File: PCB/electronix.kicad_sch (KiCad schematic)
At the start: 86 parts, among them IC1 DRV8210DRLR, IC2 DRV8210DRLR, IC3 AP9101CK6-ANTRG1, IC4 ICM-20602, J1 USB-C 6pin, J2 PRG, M1 N20 motor, M2 N20 motor, Q1 757-SSM6N7002KFULF, Q2 757-SSM6N7002KFULF, Q3 Phototransistor, Q4 Phototransistor, Q5 Phototransistor, Q6 Phototransistor, Q7 757-SSM6N7002KFULF, Q8 UMH3N FHA, SW1 RESET, U2 MCP73213-A6SI/MF, U3 ESP32-WROOM-32, U4 LMR51420YDDRCR

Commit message: Add start button General schematic edits Add Mouser BOM
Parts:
- removed R25, R26, R27: 10k, symbol Device:R
- added C22: 4u7/50V, symbol Device:C
- added D7, D8: LED, symbol Device:LED
- added R11: 100k 1%, Resistor_SMD:R_0603_1608Metric, symbol Device:R
- added R12: 22k1 1%, Resistor_SMD:R_0603_1608Metric, symbol Device:R
- added R36, R37: 330R, symbol Device:R
- added R5: 10k, symbol Device:R
- added SW2: SW_DIP_x01, symbol Switch:SW_DIP_x01
- added SW3: START, symbol Switch:SW_Push
- L1: value 4u7 -> 3u3
- renumbered C21 to C1, C3 to C10, C1 to C11, C4 to C12, C5 to C16, C6 to C17, C14 to C2, C19 to C3, C20 to C4, C17 to C5, C16 to C6, C15 to C7, C18 to C8, C2 to C9, D6 to D1, D1 to D2, D2 to D3, D3 to D5, D4 to D6, IC4 to IC1, IC3 to IC2, IC1 to IC3, IC2 to IC4, Q8 to Q1, Q7 to Q2, Q2 to Q3, Q6 to Q5, Q1 to Q6, Q3 to Q7, Q5 to Q8, R30 to R1, R23 to R10, R24 to R11, R22 to R12, R5 to R13, R7 to R14, R6 to R15, R8 to R16, R28 to R17, R1 to R18, R2 to R19, R35 to R2, R34 to R20, R33 to R21, R3 to R22, R4 to R23, R9 to R24, R10 to R25, R11 to R28, R12 to R29, R31 to R30, R32 to R31, R13 to R32, R14 to R33, R15 to R34, R16 to R35, R29 to R6, R19 to R7, R20 to R8, R21 to R9, U2 to U1, U3 to U2
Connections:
- net +3V3: now also C10.1, C5.1, C6.1, C7.2, C8.1, C9.1, D1.1 (K), IC3.5 (VM), IC4.5 (VM), M1.2 (Pin_2), M2.2 (Pin_2), R17.2, SW1.2, U4.3 (VIN), U4.5 (EN), D8.2 (A), R11.1, R5.1, SW2.1
- net +BATT: now also SW2.2; no longer C10.1, C5.1, C6.1, C7.2, C8.1, C9.1, D1.1 (K), IC3.5 (VM), IC4.5 (VM), M1.2 (Pin_2), M2.2 (Pin_2), R17.2, SW1.2, U4.3 (VIN), U4.5 (EN)
- net GND: now also C22.2, R12.2, R36.1, R37.1, SW3.1
- net v_sense: now also R11.2, R12.1
- net ST: now reaches U2.30 (IO18)
- net ST: now also C22.1, R5.2, SW3.2
- net at U2.37 (IO23): now also D7.2 (A)
- new net: D8.1 (K), R37.2
- new net: D7.1 (K), R36.2
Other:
- note added: "START"
- moved on the sheet: C2, C5, C8, D1, J2, R1, R17, R6, SW1

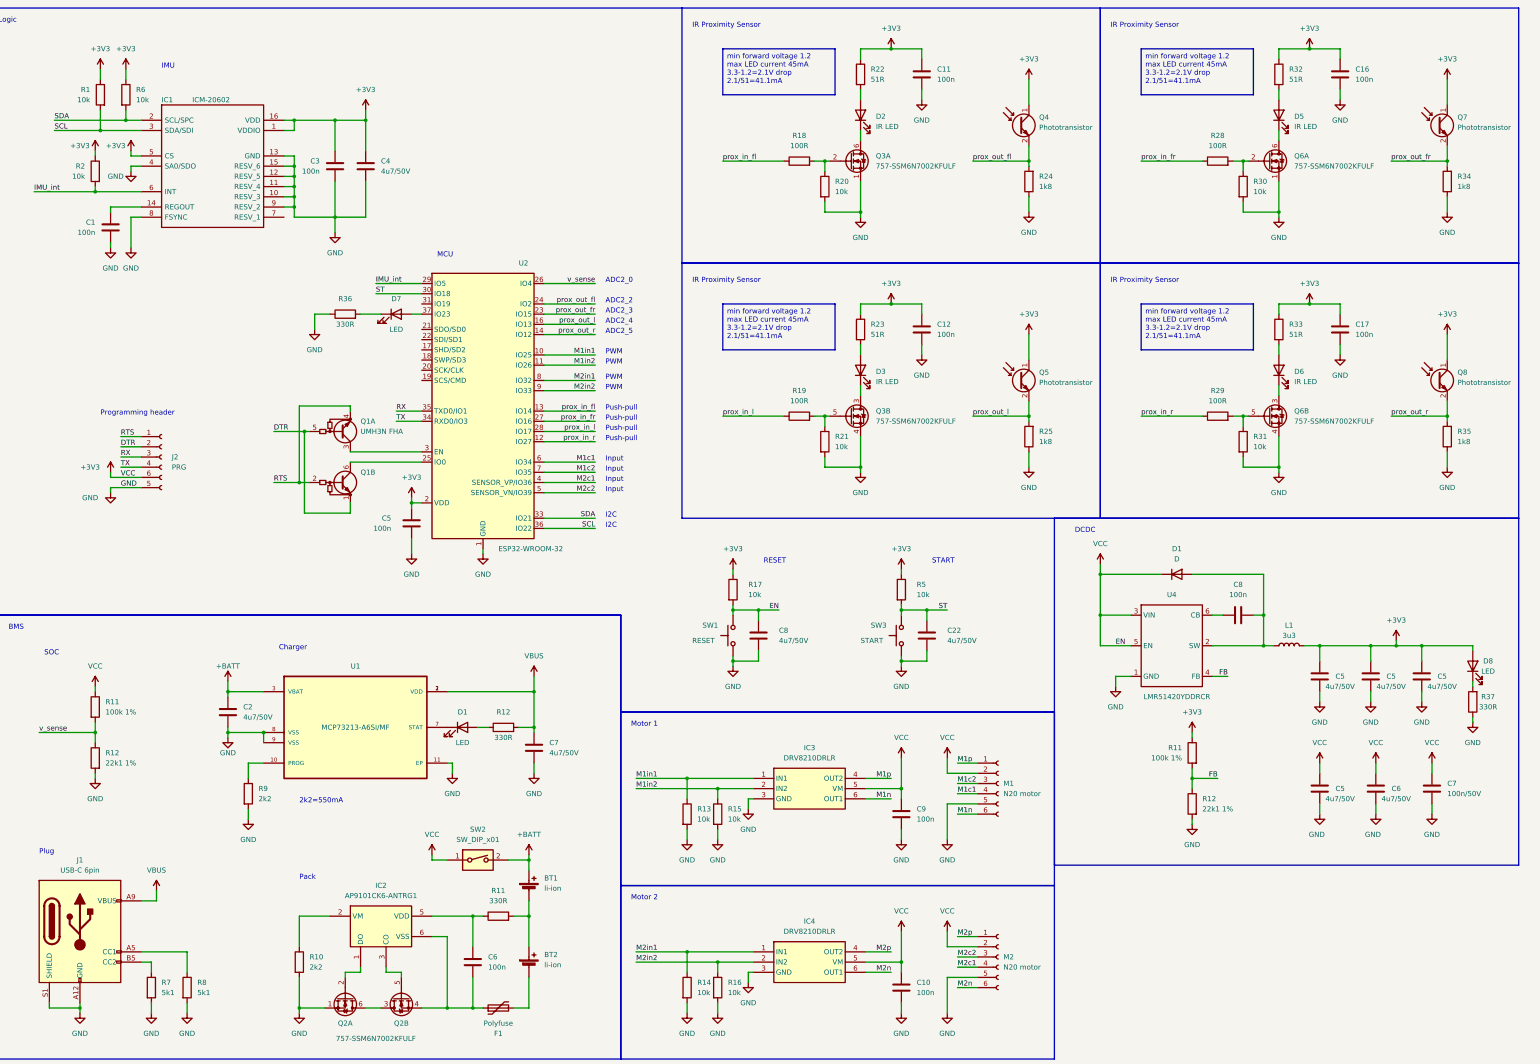
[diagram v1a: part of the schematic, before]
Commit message: Assign fooprints Finish BOM Fix libraries Generic footprints where applicable ERC - remove erroneous net labels Start working on layout
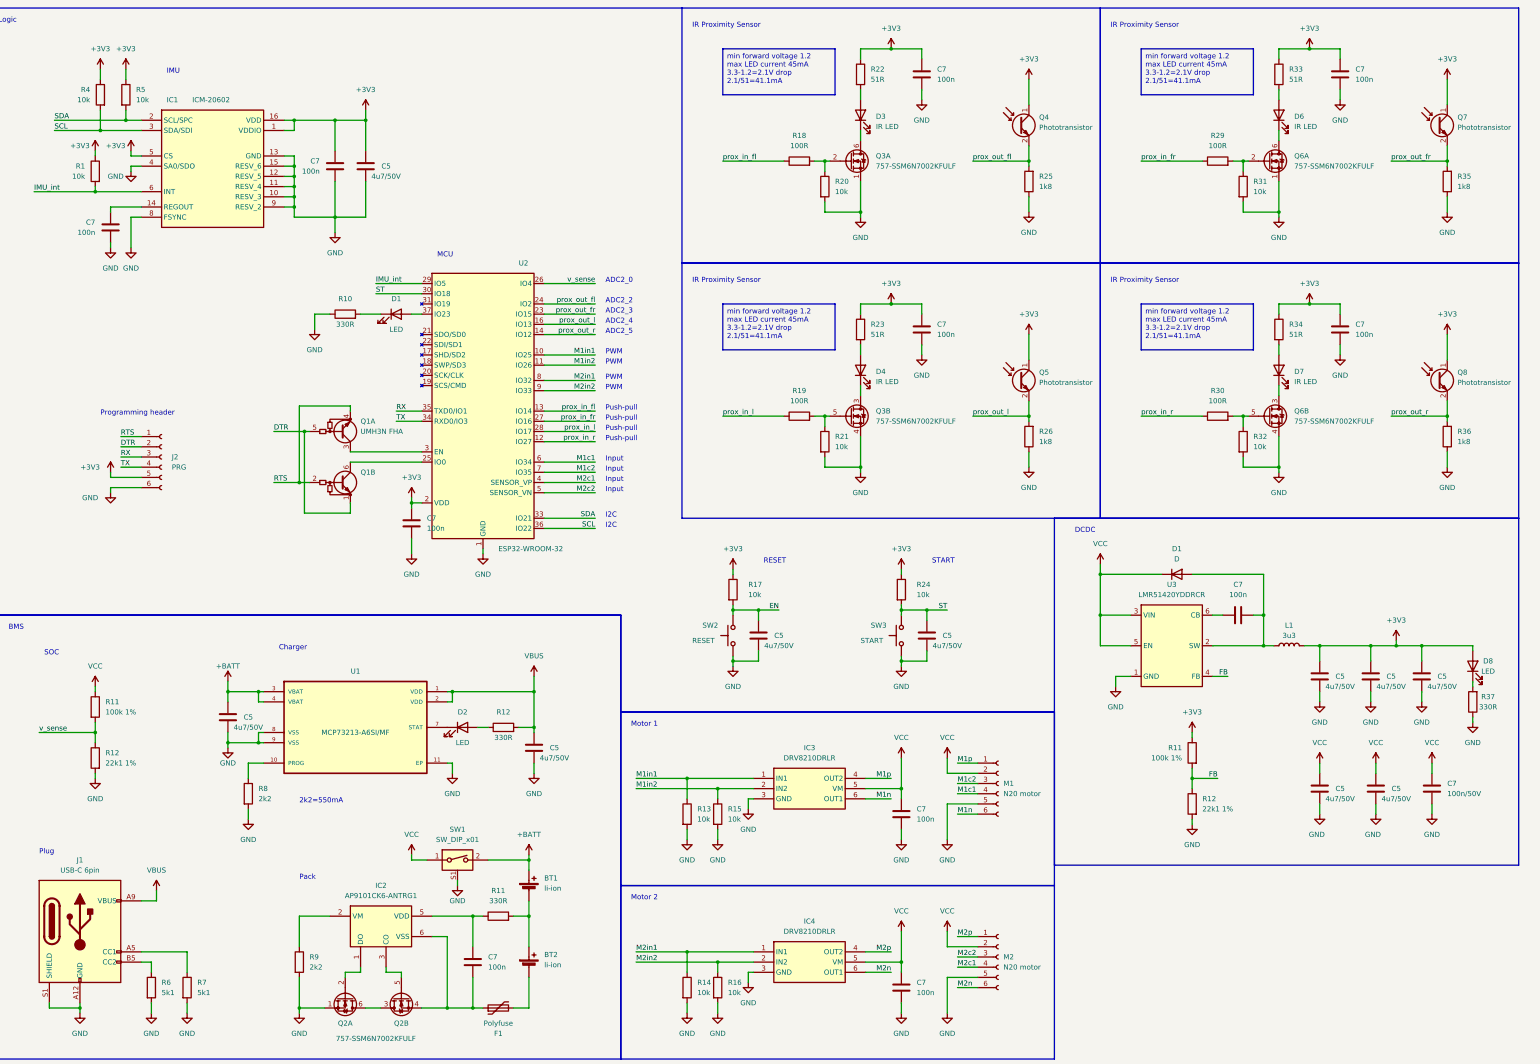
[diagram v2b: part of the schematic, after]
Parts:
- removed C1, C10, C11, C12, C16, C17, C3, C5, C6, C8, C9: 100n, symbol Device:C
- removed C2, C22, C4, C7, C8: 4u7/50V, symbol Device:C
- removed C5 (x3), C6: 4u7/50V, Capacitor_SMD:C_1206_3216Metric, symbol Device:C
- removed U4: LMR51420YDDRCR, Package_TO_SOT_SMD:SOT-23-6, symbol parts:LMR51420
- added C5 (x9): 4u7/50V, Capacitor_SMD:C_0805_2012Metric, symbol Device:C
- added C7 (x11): 100n, Capacitor_SMD:C_0603_1608Metric, symbol Device:C
- added U3: LMR51420YDDRCR, Package_TO_SOT_SMD:SOT-23-6, symbol LMR51420:LMR51420
- BT1, BT2: footprint (none) -> Connector_JST:JST_XH_B2B-XH-AM_1x02_P2.50mm_Vertical
- C5: footprint Capacitor_SMD:C_1206_3216Metric -> Capacitor_SMD:C_0805_2012Metric
- D1: renamed from D7; footprint (none) -> LED_SMD:LED_0603_1608Metric
- D2: renamed from D1; footprint (none) -> LED_SMD:LED_0603_1608Metric
- D3: renamed from D2; footprint (none) -> LED_THT:LED_D5.0mm_Horizontal_O1.27mm_Z3.0mm
- D4: renamed from D3; footprint (none) -> LED_THT:LED_D5.0mm_Horizontal_O1.27mm_Z3.0mm
- D6: renamed from D5; footprint (none) -> LED_THT:LED_D5.0mm_Horizontal_O1.27mm_Z3.0mm
- D7: renamed from D6; footprint (none) -> LED_THT:LED_D5.0mm_Horizontal_O1.27mm_Z3.0mm
- D8: footprint (none) -> LED_SMD:LED_0603_1608Metric
- F1: footprint (none) -> Fuse:Fuse_1812_4532Metric
- IC1: footprint IAM20680HP -> Package_LGA:LGA-16_3x3mm_P0.5mm
- IC2: footprint SOT95P285X140-6N -> Package_TO_SOT_SMD:SOT-23-6
- IC3, IC4: footprint SOTFL50P160X60-6N -> Package_TO_SOT_SMD:SOT-563
- J1: footprint (none) -> 10164359-00011LF:1016435900011LF
- J2: footprint (none) -> Connector_PinHeader_2.54mm:PinHeader_1x06_P2.54mm_Vertical
- L1: footprint Inductor_SMD:L_Ferrocore_DLG-0705 -> Inductor_SMD:L_Changjiang_FNR5040S
- M1, M2: footprint (none) -> Connector_JST:JST_XH_B6B-XH-AM_1x06_P2.50mm_Vertical
- Q1, Q2, Q3, Q6: footprint (none) -> Package_TO_SOT_SMD:SOT-363_SC-70-6
- Q4, Q5, Q7, Q8: footprint (none) -> LED_THT:LED_D5.0mm_Horizontal_O1.27mm_Z3.0mm_IRBlack
- R1: renamed from R2; footprint (none) -> Resistor_SMD:R_0603_1608Metric
- R10: renamed from R36; footprint (none) -> Resistor_SMD:R_0603_1608Metric
- R11, R12, R13, R14, R15, R16, R17, R18, R19, R20, R21, R22, R23, R37: footprint (none) -> Resistor_SMD:R_0603_1608Metric
- R24: renamed from R5; footprint (none) -> Resistor_SMD:R_0603_1608Metric
- R25: renamed from R24; footprint (none) -> Resistor_SMD:R_0603_1608Metric
- R26: renamed from R25; footprint (none) -> Resistor_SMD:R_0603_1608Metric
- R29: renamed from R28; footprint (none) -> Resistor_SMD:R_0603_1608Metric
- R30: renamed from R29; footprint (none) -> Resistor_SMD:R_0603_1608Metric
- R31: renamed from R30; footprint (none) -> Resistor_SMD:R_0603_1608Metric
- R32: renamed from R31; footprint (none) -> Resistor_SMD:R_0603_1608Metric
- R33: renamed from R32; footprint (none) -> Resistor_SMD:R_0603_1608Metric
- R34: renamed from R33; footprint (none) -> Resistor_SMD:R_0603_1608Metric
- R35: renamed from R34; footprint (none) -> Resistor_SMD:R_0603_1608Metric
- R36: renamed from R35; footprint (none) -> Resistor_SMD:R_0603_1608Metric
- R4: renamed from R1; footprint (none) -> Resistor_SMD:R_0603_1608Metric
- R5: renamed from R6; footprint (none) -> Resistor_SMD:R_0603_1608Metric
- R6: renamed from R7; footprint (none) -> Resistor_SMD:R_0603_1608Metric
- R7: renamed from R8; footprint (none) -> Resistor_SMD:R_0603_1608Metric
- R8: renamed from R9; footprint (none) -> Resistor_SMD:R_0603_1608Metric
- R9: renamed from R10; footprint (none) -> Resistor_SMD:R_0603_1608Metric
- SW1: renamed from SW2; footprint (none) -> 1825232-1:18252321
- SW2: renamed from SW1; footprint (none) -> PTS636_SL50_LFS:PTS636SL50LFS
- SW3: footprint (none) -> PTS636_SL50_LFS:PTS636SL50LFS
- U1: footprint SON50P300X300X100-11N -> Package_DFN_QFN:DFN-10-1EP_3x3mm_P0.5mm_EP1.65x2.38mm_ThermalVias
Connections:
- net +3V3: now also J2.5 (Pin_5), C5.1, C5.1, C5.1, C7.2, C7.2, C7.2, C7.2, C7.2, C7.2; no longer C7.2, D1.1 (K), IC3.5 (VM), IC4.5 (VM), J2.6 (Pin_6), M1.2 (Pin_2), M2.2 (Pin_2), R11.1, R17.2, SW1.1, SW2.2
- net +BATT: now also U1.4 (VBAT), C5.1
- net FB: now also U3.4 (FB)
- net GND: now also J1.S2 (SHIELD), J1.S3 (SHIELD), J1.S4 (SHIELD), J2.6 (Pin_6), SW1.S1 (SHIELD), SW1.S2 (SHIELD), C5.2, C5.2, C5.2, C5.2, C5.2, C5.2, C5.2, C5.2, C5.2, C7.1, C7.1, C7.1, C7.1, C7.1, C7.1, C7.1, C7.1, C7.1, U3.1 (GND); no longer J2.5 (Pin_5)
- net ST: now also C5.1
- net VBUS: now also C5.1
- net at D1.2 (A), L1.1: now also C7.1, U3.2 (SW)
- net at IC2.5 (VDD), R11.1: now also C7.2
- net at IC1.14 (REGOUT): now also C7.2
- net at F1.1, IC2.6 (VSS), Q2.4 (S): now also C7.1
- new net: C7.2, U3.6 (CB)
- new net EN: C5.1, R17.2, SW2.2
- new net VCC: C5.1, C5.1, C7.2, C7.2, C7.2, D1.1 (K), IC3.5 (VM), IC4.5 (VM), M1.2 (Pin_2), M2.2 (Pin_2), R11.1, SW1.1, U3.3 (VIN), U3.5 (EN)

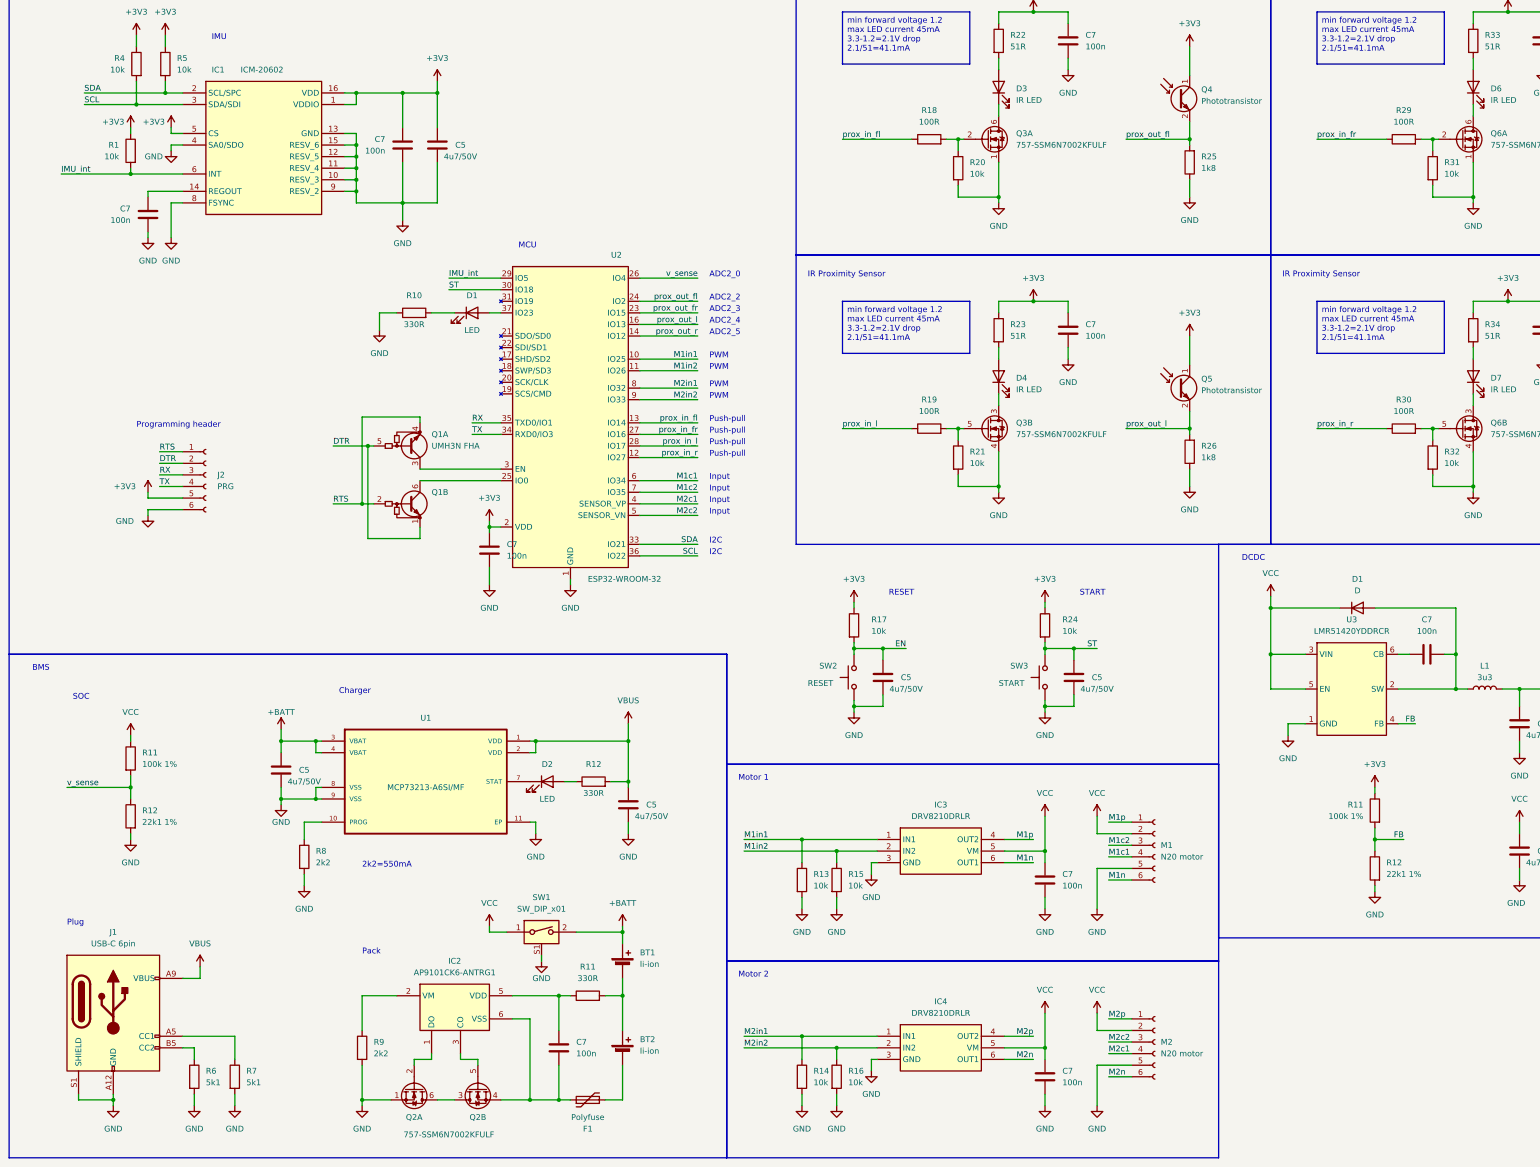
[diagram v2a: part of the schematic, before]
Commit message: Layout Add diode on prg connector remove diode on PSU to avoid driving motors from 3V3 Footprints for motors and omniwheel
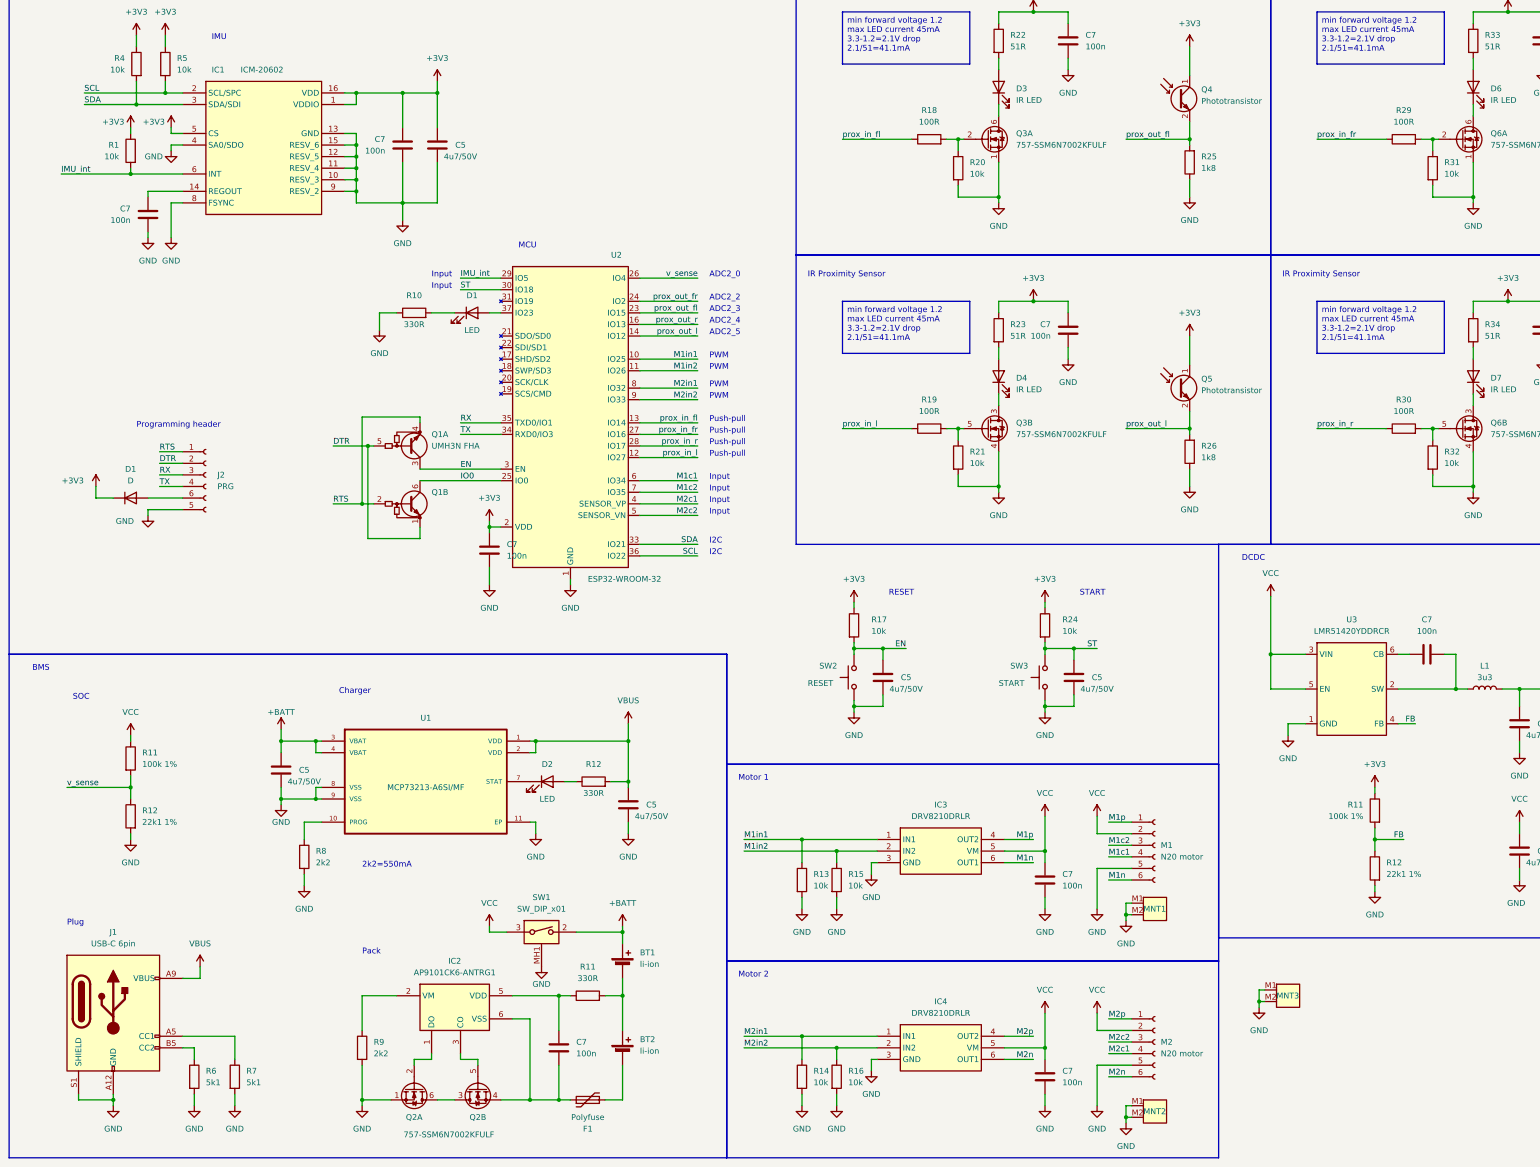
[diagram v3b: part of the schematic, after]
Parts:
- added MNT1, MNT2: ~, Custom_parts:N20 encoder motor, symbol Custom_parts:Mounting
- added MNT3: ~, Custom_parts:Ball support, symbol Custom_parts:Mounting
- BT1, BT2: footprint Connector_JST:JST_XH_B2B-XH-AM_1x02_P2.50mm_Vertical -> Connector_JST:JST_XH_B2B-XH-A_1x02_P2.50mm_Vertical
- D1: footprint Diode_SMD:D_0805_2012Metric -> Diode_SMD:D_SOD-128
- IC1: footprint Package_LGA:LGA-16_3x3mm_P0.5mm -> Package_LGA:LGA-16_3x3mm_P0.5mm_LayoutBorder3x5y
- J2: footprint Connector_PinHeader_2.54mm:PinHeader_1x06_P2.54mm_Vertical -> Connector_PinSocket_2.54mm:PinSocket_1x06_P2.54mm_Vertical
- M1, M2: footprint Connector_JST:JST_XH_B6B-XH-AM_1x06_P2.50mm_Vertical -> Connector_JST:JST_XH_B6B-XH-A_1x06_P2.50mm_Vertical
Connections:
- net +3V3: now also D1.1 (K); no longer J2.5 (Pin_5)
- net EN: now also Q1.3 (C1), U2.3 (EN)
- net GND: now also J2.5 (Pin_5), SW1.MH1 (SHIELD), SW1.MH2 (SHIELD), MNT1.M1, MNT1.M2, MNT2.M1, MNT2.M2, MNT3.M1, MNT3.M2; no longer J2.6 (Pin_6), SW1.S1 (SHIELD), SW1.S2 (SHIELD)
- net SCL: now also IC1.2 (SCL/SPC), R5.2; no longer IC1.3 (SDA/SDI), R4.2
- net SDA: now also IC1.3 (SDA/SDI), R4.2; no longer IC1.2 (SCL/SPC), R5.2
- net VCC: now also SW1.3; no longer D1.1 (K), SW1.1
- net prox_in_l: now also U2.12 (IO27); no longer U2.28 (IO17)
- net prox_in_r: now also U2.28 (IO17); no longer U2.12 (IO27)
- net prox_out_fl: now also U2.23 (IO15); no longer U2.24 (IO2)
- net prox_out_fr: now also U2.24 (IO2); no longer U2.23 (IO15)
- net prox_out_l: now also U2.14 (IO12); no longer U2.16 (IO13)
- net prox_out_r: now also U2.16 (IO13); no longer U2.14 (IO12)
- net at C7.1, L1.1, U3.2 (SW): no longer D1.2 (A)
- net IO0: now reaches Q1.6 (C1), U2.25 (IO0)
- new net: D1.2 (A), J2.6 (Pin_6)
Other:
- moved on the sheet: C7, SW1
